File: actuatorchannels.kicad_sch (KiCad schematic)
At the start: 102 parts, among them J10 ACT CH9, J11 ACT CH10, J12 ACT CH11, J13 ACT CH12, J14 ACT CH13, J15 ACT CH14, J16 ACT CH15, J17 ACT CH16, J2 ACT CH1, J3 ACT CH2, J4 ACT CH3, J5 ACT CH4, J6 ACT CH5, J7 ACT CH6, J8 ACT CH7, J9 ACT CH8, U10 TLP241A, U11 TLP241A, U12 TLP241A, U13 TLP241A, U14 TLP241A, U15 TLP241A, U16 TLP241A, U17 TLP241A, U18 TLP241A, U19 PCA9534, U20 PCA9534, U3 TLP241A, U4 TLP241A, U5 TLP241A, U6 TLP241A, U7 TLP241A, U8 TLP241A, U9 TLP241A

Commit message: MPN reassignment
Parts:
- J10, J11, J12, J13, J14, J15, J16, J17, J2, J3, J4, J5, J6, J7, J8, J9: footprint TerminalBlock_Phoenix:TerminalBlock_Phoenix_PT-1,5-2-5.0-H_1x02_P5.00mm_Horizontal -> actuation:1989447

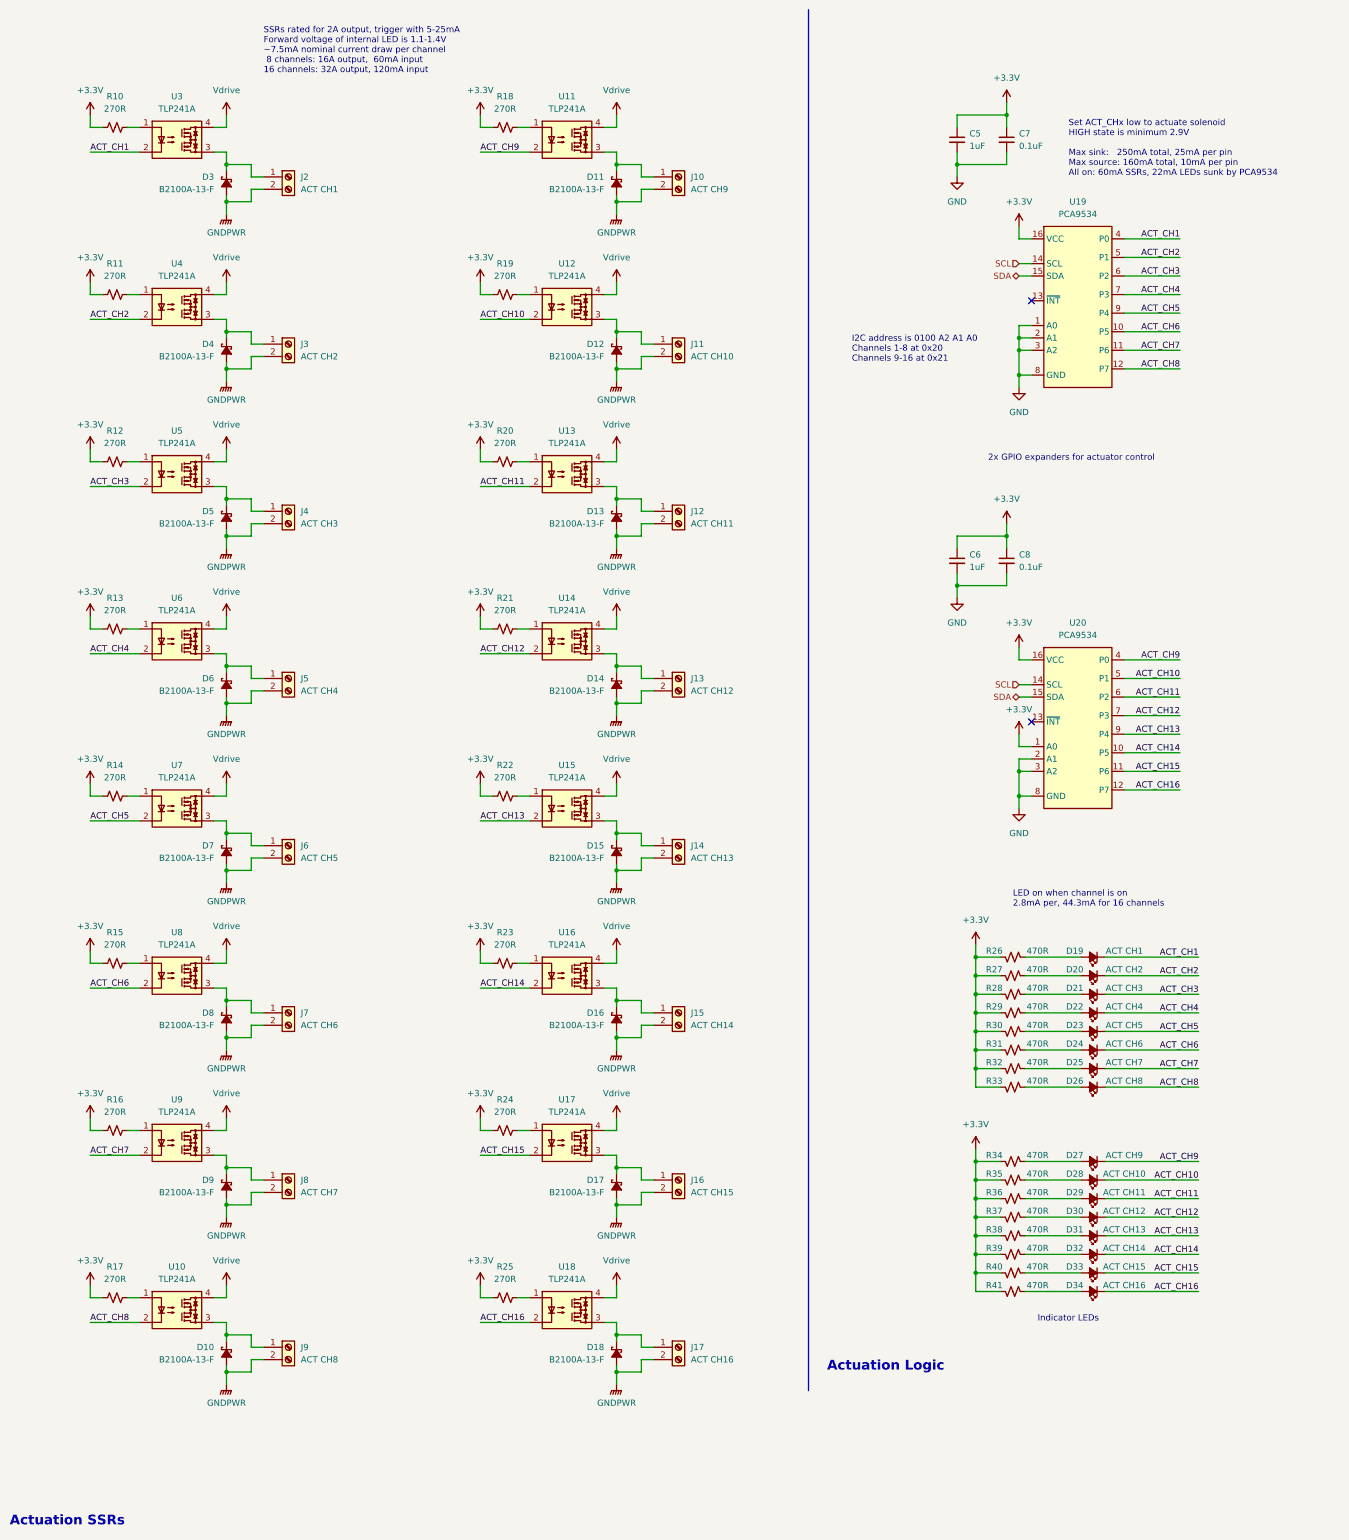
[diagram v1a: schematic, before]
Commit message: Check-safe channel, footprint changes
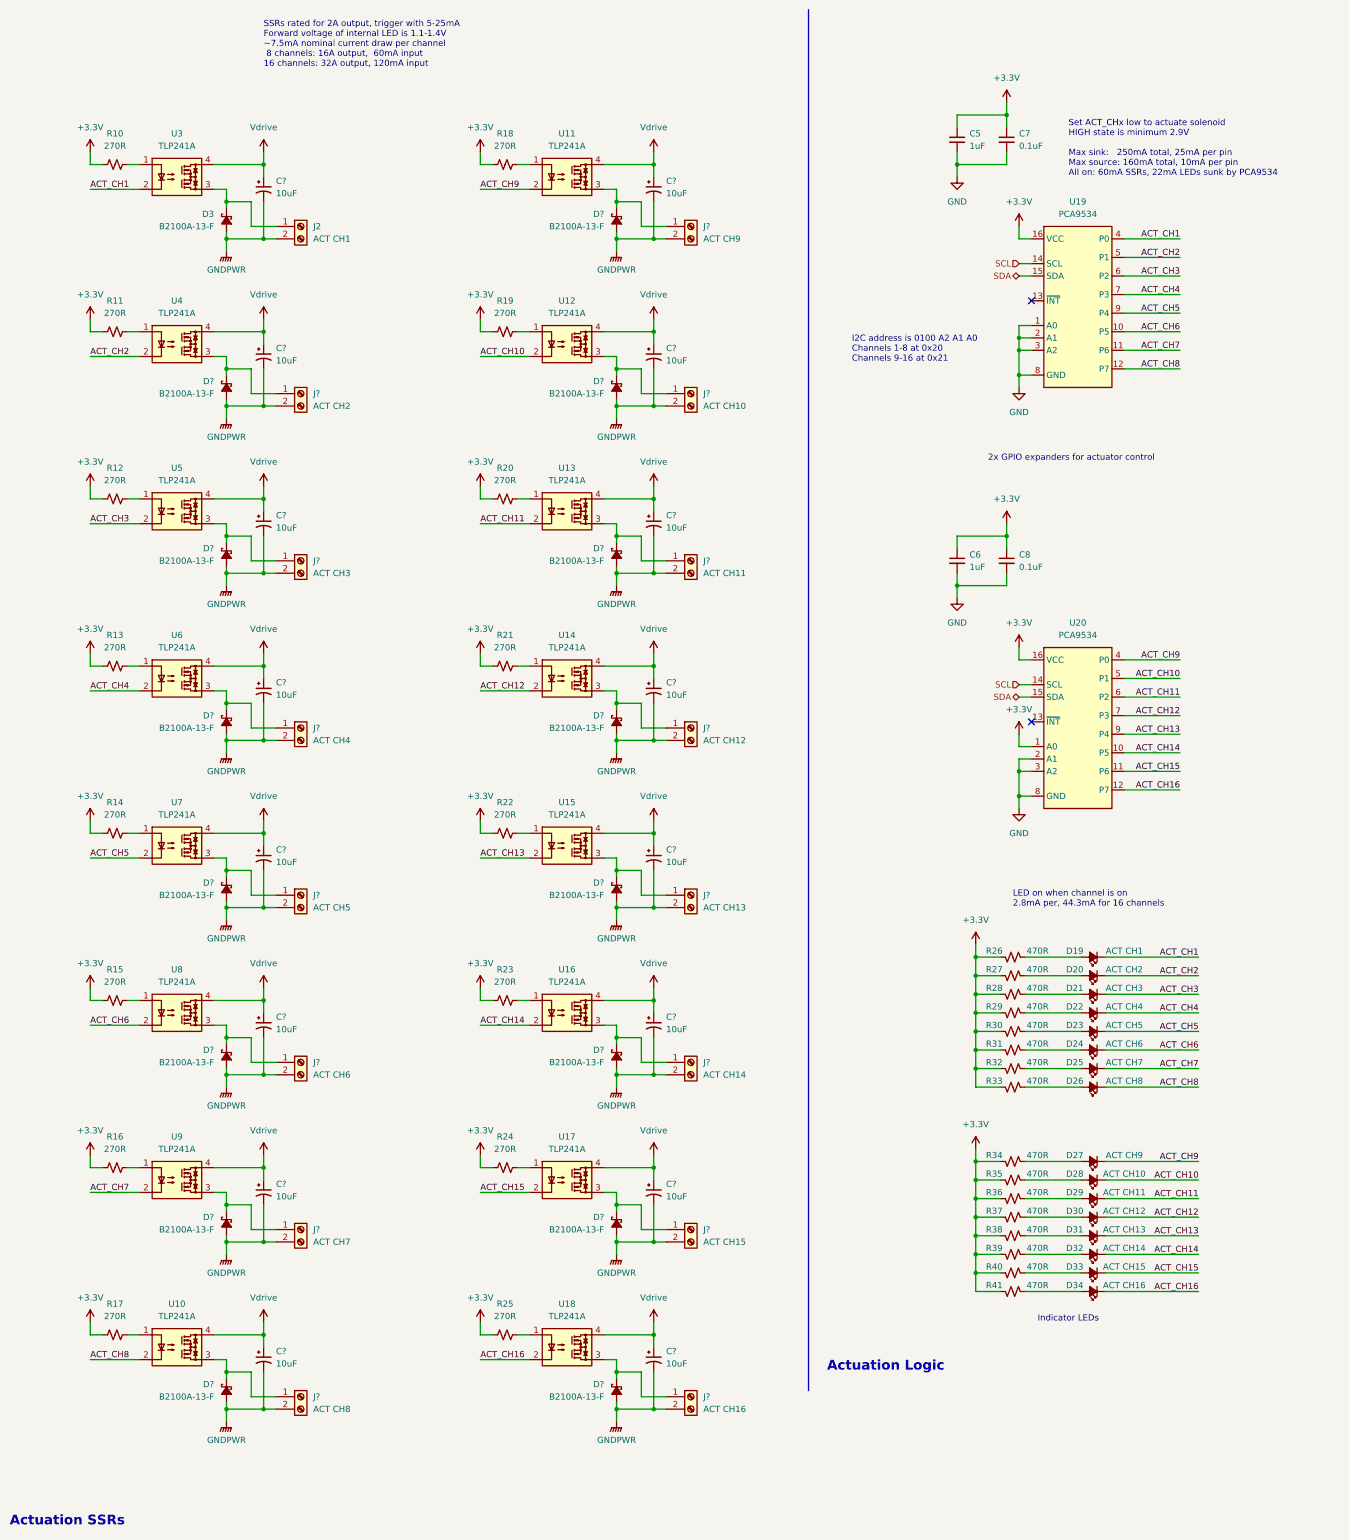
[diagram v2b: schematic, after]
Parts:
- removed D10, D11, D12, D13, D14, D15, D16, D17, D18, D4, D5, D6, D7, D8, D9: B2100A-13-F, Diode_SMD:D_SMA, symbol Device:D_Schottky_Small_Filled
- removed J10: ACT CH9, actuation:1989447, symbol Connector:Screw_Terminal_01x02
- removed J11: ACT CH10, actuation:1989447, symbol Connector:Screw_Terminal_01x02
- removed J12: ACT CH11, actuation:1989447, symbol Connector:Screw_Terminal_01x02
- removed J13: ACT CH12, actuation:1989447, symbol Connector:Screw_Terminal_01x02
- removed J14: ACT CH13, actuation:1989447, symbol Connector:Screw_Terminal_01x02
- removed J15: ACT CH14, actuation:1989447, symbol Connector:Screw_Terminal_01x02
- removed J16: ACT CH15, actuation:1989447, symbol Connector:Screw_Terminal_01x02
- removed J17: ACT CH16, actuation:1989447, symbol Connector:Screw_Terminal_01x02
- removed J3: ACT CH2, actuation:1989447, symbol Connector:Screw_Terminal_01x02
- removed J4: ACT CH3, actuation:1989447, symbol Connector:Screw_Terminal_01x02
- removed J5: ACT CH4, actuation:1989447, symbol Connector:Screw_Terminal_01x02
- removed J6: ACT CH5, actuation:1989447, symbol Connector:Screw_Terminal_01x02
- removed J7: ACT CH6, actuation:1989447, symbol Connector:Screw_Terminal_01x02
- removed J8: ACT CH7, actuation:1989447, symbol Connector:Screw_Terminal_01x02
- removed J9: ACT CH8, actuation:1989447, symbol Connector:Screw_Terminal_01x02
- added C? (x16): 10uF, Capacitor_SMD:CP_Elec_4x5.8, symbol Device:C_Polarized_Small_US
- added D? (x15): B2100A-13-F, Diode_SMD:D_SMA, symbol Device:D_Schottky_Small_Filled
- added J?: ACT CH5, Connector_AMASS:AMASS_XT30U-M_1x02_P5.0mm_Vertical, symbol Connector:Screw_Terminal_01x02
- added J?: ACT CH2, Connector_AMASS:AMASS_XT30U-M_1x02_P5.0mm_Vertical, symbol Connector:Screw_Terminal_01x02
- added J?: ACT CH10, Connector_AMASS:AMASS_XT30U-M_1x02_P5.0mm_Vertical, symbol Connector:Screw_Terminal_01x02
- added J?: ACT CH6, Connector_AMASS:AMASS_XT30U-M_1x02_P5.0mm_Vertical, symbol Connector:Screw_Terminal_01x02
- added J?: ACT CH16, Connector_AMASS:AMASS_XT30U-M_1x02_P5.0mm_Vertical, symbol Connector:Screw_Terminal_01x02
- added J?: ACT CH7, Connector_AMASS:AMASS_XT30U-M_1x02_P5.0mm_Vertical, symbol Connector:Screw_Terminal_01x02
- added J?: ACT CH11, Connector_AMASS:AMASS_XT30U-M_1x02_P5.0mm_Vertical, symbol Connector:Screw_Terminal_01x02
- added J?: ACT CH3, Connector_AMASS:AMASS_XT30U-M_1x02_P5.0mm_Vertical, symbol Connector:Screw_Terminal_01x02
- added J?: ACT CH9, Connector_AMASS:AMASS_XT30U-M_1x02_P5.0mm_Vertical, symbol Connector:Screw_Terminal_01x02
- added J?: ACT CH12, Connector_AMASS:AMASS_XT30U-M_1x02_P5.0mm_Vertical, symbol Connector:Screw_Terminal_01x02
- added J?: ACT CH15, Connector_AMASS:AMASS_XT30U-M_1x02_P5.0mm_Vertical, symbol Connector:Screw_Terminal_01x02
- added J?: ACT CH4, Connector_AMASS:AMASS_XT30U-M_1x02_P5.0mm_Vertical, symbol Connector:Screw_Terminal_01x02
- added J?: ACT CH8, Connector_AMASS:AMASS_XT30U-M_1x02_P5.0mm_Vertical, symbol Connector:Screw_Terminal_01x02
- added J?: ACT CH13, Connector_AMASS:AMASS_XT30U-M_1x02_P5.0mm_Vertical, symbol Connector:Screw_Terminal_01x02
- added J?: ACT CH14, Connector_AMASS:AMASS_XT30U-M_1x02_P5.0mm_Vertical, symbol Connector:Screw_Terminal_01x02
- J2: footprint actuation:1989447 -> Connector_AMASS:AMASS_XT30U-M_1x02_P5.0mm_Vertical; MPN 1989447 -> XT30U-M
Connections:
- net GNDPWR: now also C?.2, C?.2, C?.2, C?.2, C?.2, C?.2, C?.2, C?.2, C?.2, C?.2, C?.2, C?.2, C?.2, C?.2, C?.2, C?.2, D?.2 (A), D?.2 (A), D?.2 (A), D?.2 (A), D?.2 (A), D?.2 (A), D?.2 (A), D?.2 (A), D?.2 (A), D?.2 (A), D?.2 (A), D?.2 (A), D?.2 (A), D?.2 (A), D?.2 (A), J?.2 (Pin_2), J?.2 (Pin_2), J?.2 (Pin_2), J?.2 (Pin_2), J?.2 (Pin_2), J?.2 (Pin_2), J?.2 (Pin_2), J?.2 (Pin_2), J?.2 (Pin_2), J?.2 (Pin_2), J?.2 (Pin_2), J?.2 (Pin_2), J?.2 (Pin_2), J?.2 (Pin_2), J?.2 (Pin_2)
- net Vdrive: now also C?.1, C?.1, C?.1, C?.1, C?.1, C?.1, C?.1, C?.1, C?.1, C?.1, C?.1, C?.1, C?.1, C?.1, C?.1, C?.1
- net at U9.3: now also D?.1 (K), J?.1 (Pin_1)
- net at U5.3: now also D?.1 (K), J?.1 (Pin_1)
- net at U16.3: now also D?.1 (K), J?.1 (Pin_1)
- net at U11.3: now also D?.1 (K), J?.1 (Pin_1)
- net at U4.3: now also D?.1 (K), J?.1 (Pin_1)
- net at U10.3: now also D?.1 (K), J?.1 (Pin_1)
- net at U14.3: now also D?.1 (K), J?.1 (Pin_1)
- net at U6.3: now also D?.1 (K), J?.1 (Pin_1)
- net at U15.3: now also D?.1 (K), J?.1 (Pin_1)
- net at U17.3: now also D?.1 (K), J?.1 (Pin_1)
- net at U13.3: now also D?.1 (K), J?.1 (Pin_1)
- net at U18.3: now also D?.1 (K), J?.1 (Pin_1)
- net at U7.3: now also D?.1 (K), J?.1 (Pin_1)
- net at U12.3: now also D?.1 (K), J?.1 (Pin_1)
- net at U8.3: now also D?.1 (K), J?.1 (Pin_1)
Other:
- moved on the sheet: D3, J2, R10, R11, R12, R13, R14, R15, R16, R17, R18, R19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

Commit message: Test pads and TVS diode for drive voltage
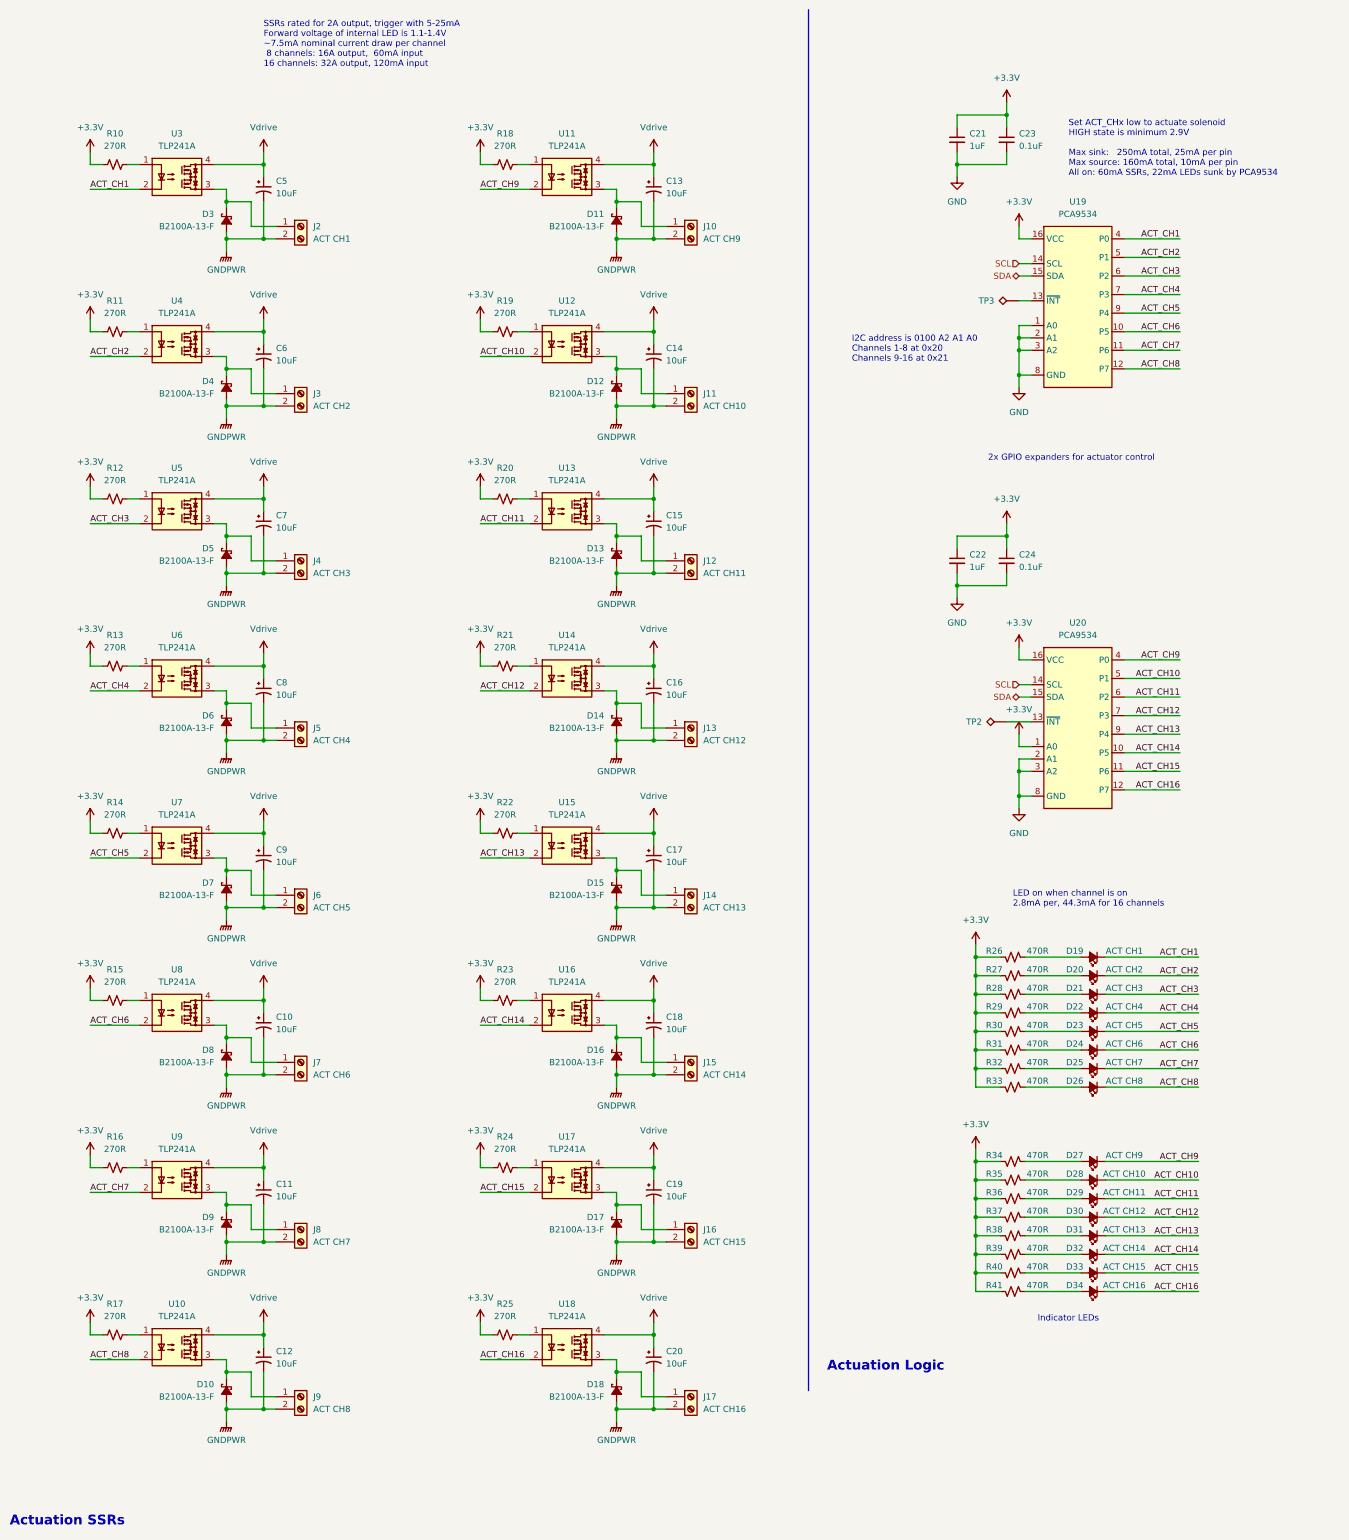
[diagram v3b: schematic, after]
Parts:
- added TP2, TP3: TestPoint_Alt, TestPoint:TestPoint_Pad_D2.0mm, symbol Connector:TestPoint_Alt
- gave numbers to parts that had none: 46
- renumbered C5 to C21, C6 to C22, C7 to C23, C8 to C24
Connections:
- net at U19.13 (~{INT}): now also TP3.1
- net at U20.13 (~{INT}): now also TP2.1
- no-connect marks 2 -> 0

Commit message: 3D models, footprint updates, general board layout
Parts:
- J10, J11, J12, J13, J14, J15, J16, J17, J2, J3, J4, J5, J6, J7, J8, J9: footprint Connector_AMASS:AMASS_XT30U-M_1x02_P5.0mm_Vertical -> actuation:XT30U-M
